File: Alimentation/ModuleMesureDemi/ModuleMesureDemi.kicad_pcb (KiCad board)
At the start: 4 copper layers, 55.8 x 51.8 mm, 62 parts, among them J1 5V, J10 I2C SDA, J11 SWD, J12 ARIG Interf, J5 Out Mes 1, J6 Out Mes 2, J7 In Mes 1, J8 In Mes 2, J9 I2C SCL, Q1 BSS138, Q2 BSS138, SW1 Reset, SW2 Boot0, SW3 Boot1, U3 ACS711xEXLT-15AB, U4 ACS711xEXLT-15AB, U5 AMS1117-3.3, U6 STM32F103C8Tx, Y1 16Mhz

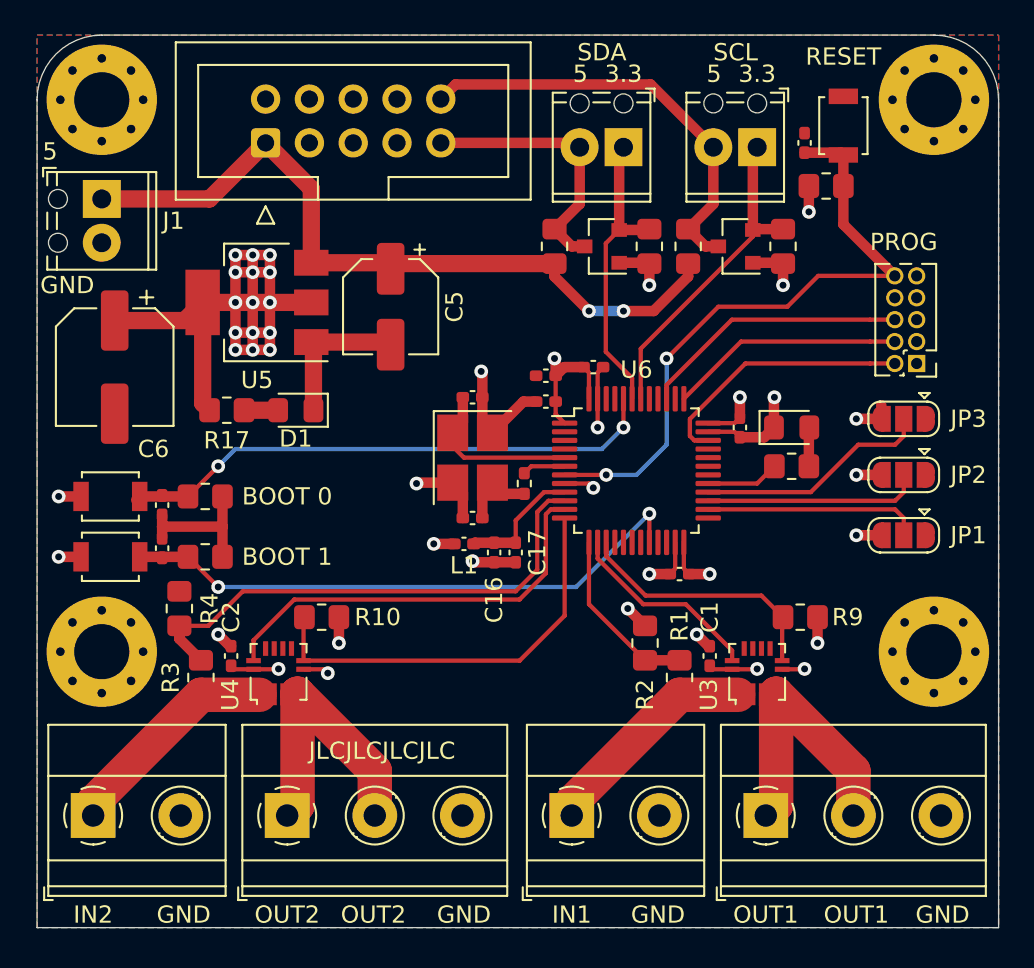
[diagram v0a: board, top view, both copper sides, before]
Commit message: Upgrade AlimMesureDemi to Kicad 7
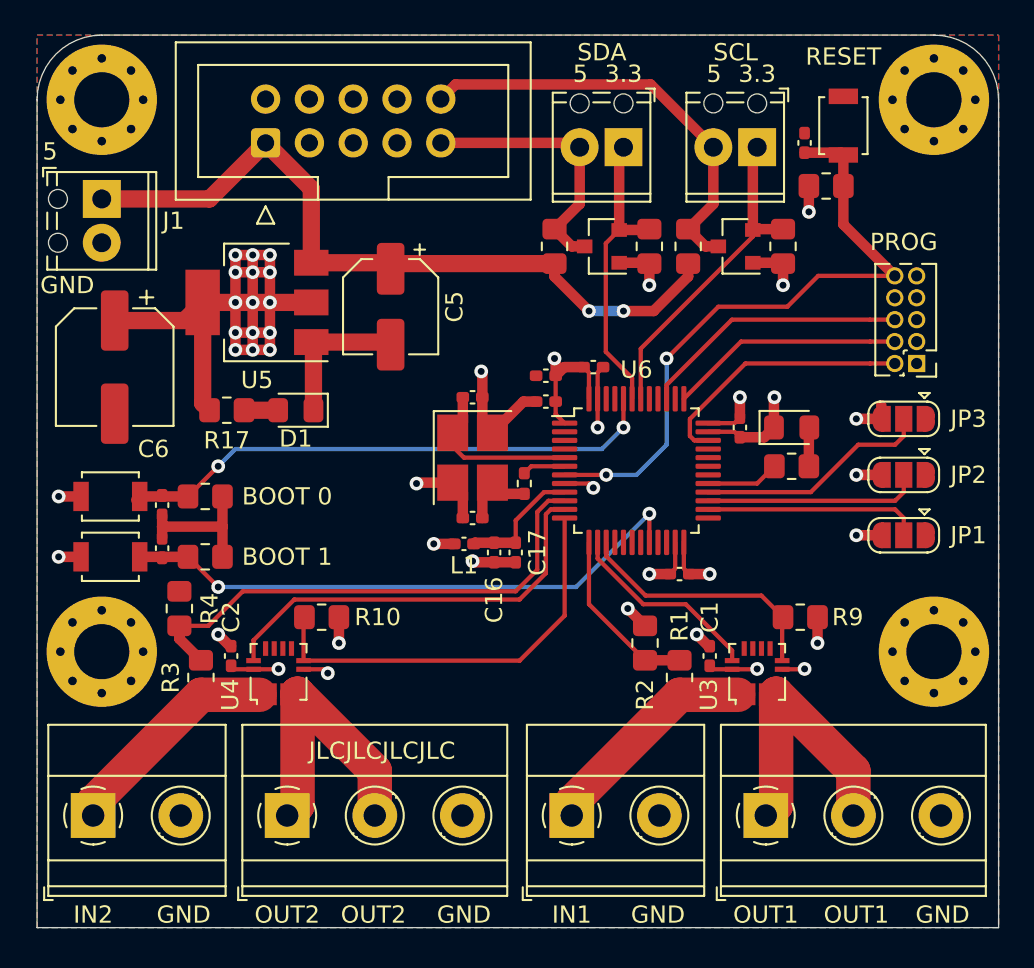
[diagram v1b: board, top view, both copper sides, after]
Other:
- net class Default removed
